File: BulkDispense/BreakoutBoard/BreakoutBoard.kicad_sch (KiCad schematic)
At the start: 30 parts, among them J1 PS, J10 R0~R5, J11 WL1, J12 WL2, J13 DigitalOUT 0~3, J14 DigitalOUT 4~7, J15 WB1, J16 WB2, J17 AnalogIOs, J18 WB-MV1&2, J19 WB-MV3&4, J2 MV1&2, J20 FS1, J21 FS2~FS4, J22 WB-MV5&6, J24 LDS, J3 MV3&4, J4 RV1~4, J5 PCV, J6 FS1, J7 FS3, J8 FS2, J9 FS4

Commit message: Add updated layout
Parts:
- removed J11: WL1, PartsLibrary:CONN_37203-62A3-003PL_3MM, symbol Connector:Conn_01x03_Socket
- removed J12: WL2, PartsLibrary:CONN_37203-62A3-003PL_3MM, symbol Connector:Conn_01x03_Socket
- removed J15: WB1, PartsLibrary:CONN_37203-62A3-003PL_3MM, symbol Connector:Conn_01x03_Socket
- removed J16: WB2, PartsLibrary:CONN_37203-62A3-003PL_3MM, symbol Connector:Conn_01x03_Socket
- removed J22: WB-MV5&6, PartsLibrary:CONN_37203-62A3-003PL_3MM, symbol Connector:Conn_01x03_Socket
- added J11: WL1, PartsLibrary:CONN_37204-62A3-004PL_3MM, symbol Connector:Conn_01x04_Socket
- added J12: WL2, PartsLibrary:CONN_37204-62A3-004PL_3MM, symbol Connector:Conn_01x04_Socket
- added J15: WB1, PartsLibrary:CONN_37204-62A3-004PL_3MM, symbol Connector:Conn_01x04_Socket
- added J16: WB2, PartsLibrary:CONN_37204-62A3-004PL_3MM, symbol Connector:Conn_01x04_Socket
- added J22: WB-MV5&6, PartsLibrary:CONN_37204-62A3-004PL_3MM, symbol Connector:Conn_01x04_Socket
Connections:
- net +24V: now also J11.1 (Pin_1), J12.1 (Pin_1), J15.1 (Pin_1), J16.1 (Pin_1)
- net AI4: now also J15.3 (Pin_3)
- net AI5: now also J16.3 (Pin_3)
- net AI6: now also J11.3 (Pin_3)
- net AI7: now also J12.3 (Pin_3)
- net GND: now also J11.2 (Pin_2), J12.2 (Pin_2), J15.2 (Pin_2), J16.2 (Pin_2)
- net R4_OUT: now also J22.1 (Pin_1)
- net R5_OUT: now also J22.3 (Pin_3)
- no-connect marks 2 -> 7

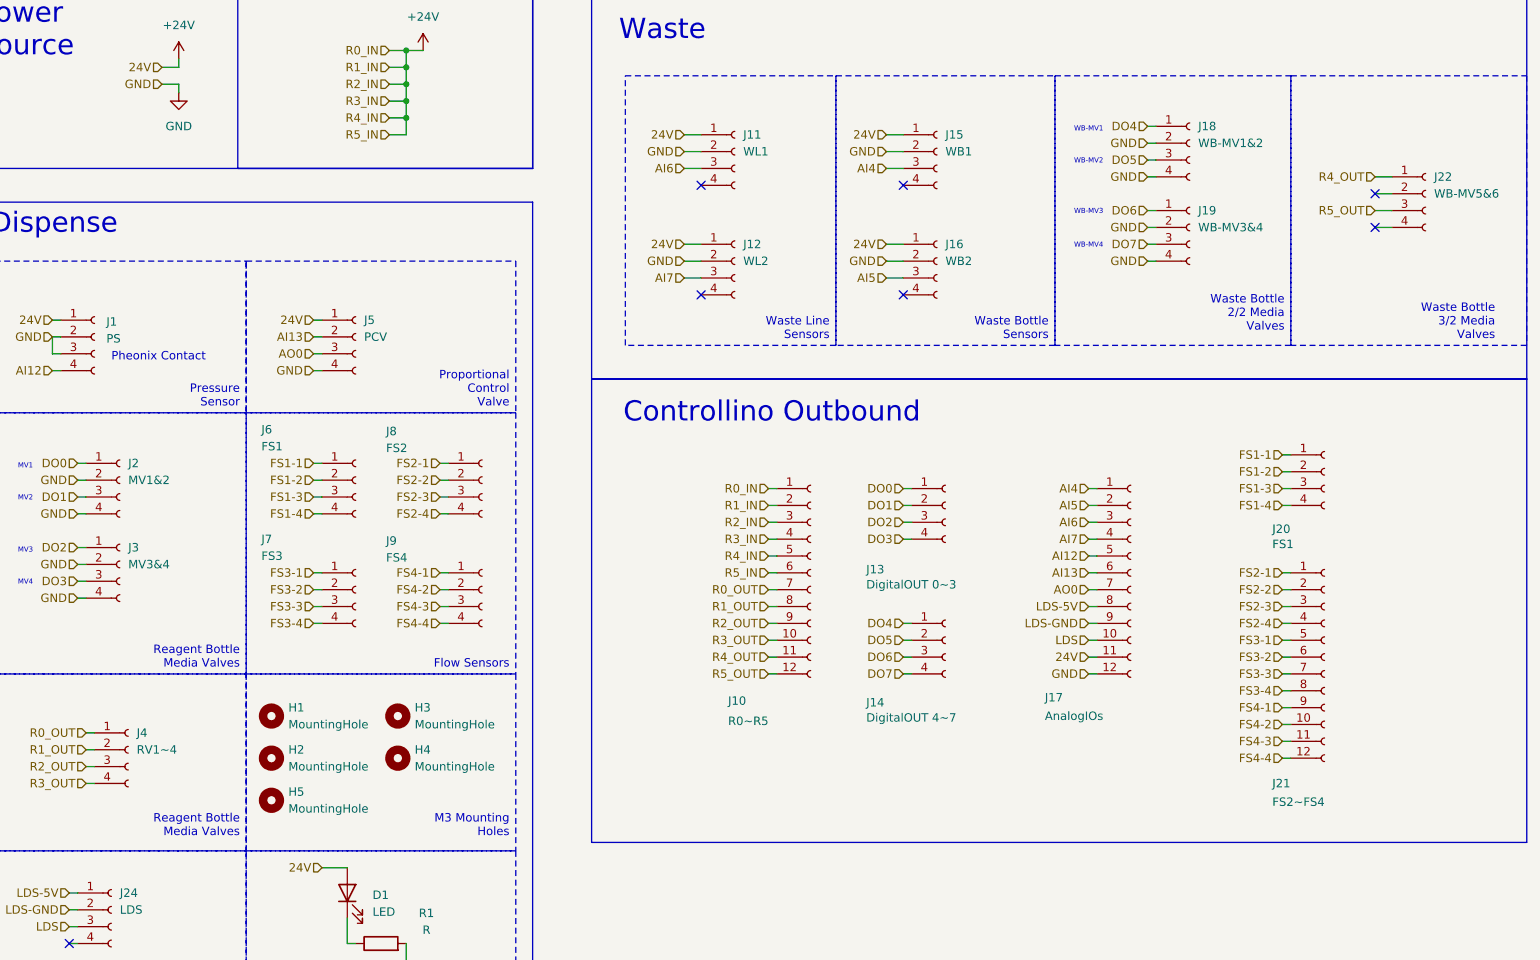
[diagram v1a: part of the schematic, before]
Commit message: Add PCB Revisions
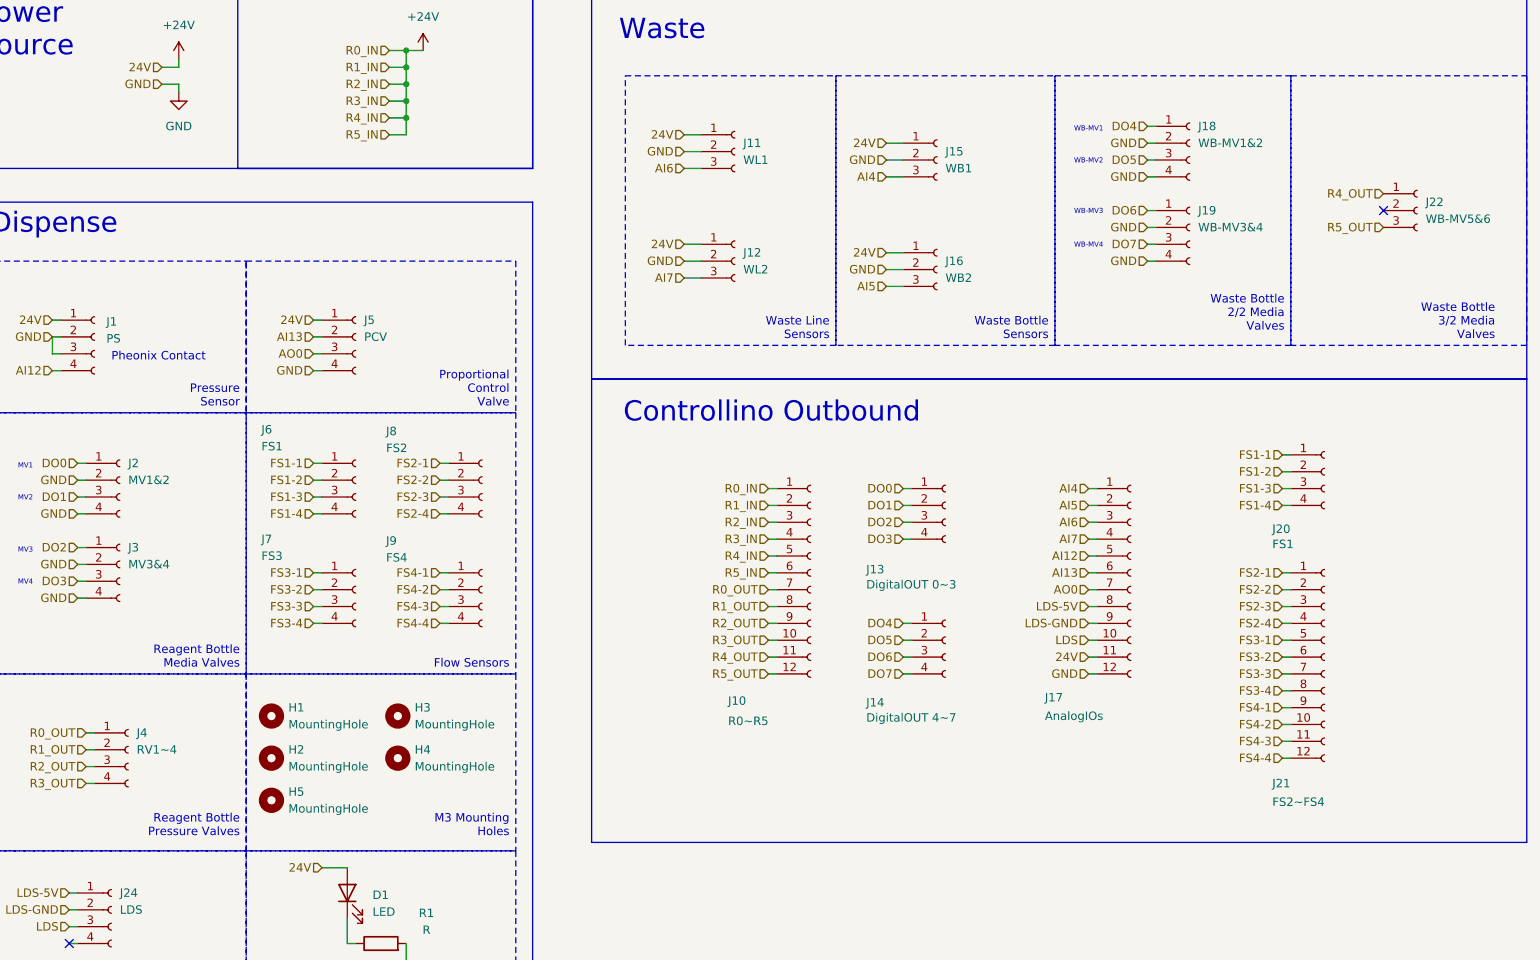
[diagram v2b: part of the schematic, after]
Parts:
- removed J11: WL1, PartsLibrary:CONN_37204-62A3-004PL_3MM, symbol Connector:Conn_01x04_Socket
- removed J12: WL2, PartsLibrary:CONN_37204-62A3-004PL_3MM, symbol Connector:Conn_01x04_Socket
- removed J15: WB1, PartsLibrary:CONN_37204-62A3-004PL_3MM, symbol Connector:Conn_01x04_Socket
- removed J16: WB2, PartsLibrary:CONN_37204-62A3-004PL_3MM, symbol Connector:Conn_01x04_Socket
- removed J22: WB-MV5&6, PartsLibrary:CONN_37204-62A3-004PL_3MM, symbol Connector:Conn_01x04_Socket
- added J11: WL1, PartsLibrary:CONN_37203-62A3-003PL_3MM, symbol Connector:Conn_01x03_Socket
- added J12: WL2, PartsLibrary:CONN_37203-62A3-003PL_3MM, symbol Connector:Conn_01x03_Socket
- added J15: WB1, PartsLibrary:CONN_37203-62A3-003PL_3MM, symbol Connector:Conn_01x03_Socket
- added J16: WB2, PartsLibrary:CONN_37203-62A3-003PL_3MM, symbol Connector:Conn_01x03_Socket
- added J22: WB-MV5&6, PartsLibrary:CONN_37203-62A3-003PL_3MM, symbol Connector:Conn_01x03_Socket
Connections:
- net +24V: now also J11.1 (Pin_1), J12.1 (Pin_1), J15.1 (Pin_1), J16.1 (Pin_1)
- net AI4: now also J15.3 (Pin_3)
- net AI5: now also J16.3 (Pin_3)
- net AI6: now also J11.3 (Pin_3)
- net AI7: now also J12.3 (Pin_3)
- net GND: now also J11.2 (Pin_2), J12.2 (Pin_2), J15.2 (Pin_2), J16.2 (Pin_2)
- net R4_OUT: now also J22.1 (Pin_1)
- net R5_OUT: now also J22.3 (Pin_3)
- no-connect marks 7 -> 2

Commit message: Add New Design
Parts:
- removed J10: R0~R5, PartsLibrary:CONN_37212-62M3-003PL_3MM, symbol Connector:Conn_01x12_Socket
- removed J13: DigitalOUT 0~3, PartsLibrary:CONN_37204-62A3-004PL_3MM, symbol Connector:Conn_01x04_Socket
- removed J14: DigitalOUT 4~7, PartsLibrary:CONN_37204-62A3-004PL_3MM, symbol Connector:Conn_01x04_Socket
- removed J17: AnalogIOs, PartsLibrary:CONN_37212-62M3-003PL_3MM, symbol Connector:Conn_01x12_Socket
- removed J18: WB-MV1&2, PartsLibrary:CONN_37204-62A3-004PL_3MM, symbol Connector:Conn_01x04_Socket
- removed J19: WB-MV3&4, PartsLibrary:CONN_37204-62A3-004PL_3MM, symbol Connector:Conn_01x04_Socket
- removed J2: MV1&2, PartsLibrary:CONN_37204-62A3-004PL_3MM, symbol Connector:Conn_01x04_Socket
- removed J20, J6: FS1, PartsLibrary:CONN_37204-62A3-004PL_3MM, symbol Connector:Conn_01x04_Socket
- removed J21: FS2~FS4, PartsLibrary:CONN_37212-62M3-003PL_3MM, symbol Connector:Conn_01x12_Socket
- removed J22: WB-MV5&6, PartsLibrary:CONN_37203-62A3-003PL_3MM, symbol Connector:Conn_01x03_Socket
- removed J24: LDS, PartsLibrary:CONN_37204-62A3-004PL_3MM, symbol Connector:Conn_01x04_Socket
- removed J3: MV3&4, PartsLibrary:CONN_37204-62A3-004PL_3MM, symbol Connector:Conn_01x04_Socket
- removed J4: RV1~4, PartsLibrary:CONN_37204-62A3-004PL_3MM, symbol Connector:Conn_01x04_Socket
- removed J7: FS3, PartsLibrary:CONN_37204-62A3-004PL_3MM, symbol Connector:Conn_01x04_Socket
- removed J8: FS2, PartsLibrary:CONN_37204-62A3-004PL_3MM, symbol Connector:Conn_01x04_Socket
- removed J9: FS4, PartsLibrary:CONN_37204-62A3-004PL_3MM, symbol Connector:Conn_01x04_Socket
- added C1: 10uF, symbol Device:C
- added C10, C11, C4, C7: 22uF, symbol Device:C
- added C2, C6: 0.1uF, symbol Device:C
- added C3, C5, C8, C9: 4.7uF, symbol Device:C
- added D3, D4: LED, LED_SMD:LED_0201_0603Metric, symbol Device:LED
- added J10: FS1, symbol Connector:Conn_01x06_Socket
- added J13: FS2, symbol Connector:Conn_01x06_Socket
- added J14: FS3, symbol Connector:Conn_01x06_Socket
- added J17: FS4, symbol Connector:Conn_01x06_Socket
- added J20: WB1, PartsLibrary:CONN_37203-62A3-003PL_3MM, symbol Connector:Conn_01x03_Socket
- added J24: WB-MV5, PartsLibrary:CONN_37203-62A3-003PL_3MM, symbol Connector:Conn_01x03_Socket
- added J32: I2C-1, symbol Connector:Conn_01x04_Pin
- added J33: I2C-3, symbol Connector:Conn_01x04_Pin
- added J34: I2C-2, symbol Connector:Conn_01x04_Pin
- added J35: I2C-4, symbol Connector:Conn_01x04_Pin
- added J36: WB-MV6, PartsLibrary:CONN_37203-62A3-003PL_3MM, symbol Connector:Conn_01x03_Socket
- added J37: RV1, PartsLibrary:CONN_37203-62A3-003PL_3MM, symbol Connector:Conn_01x03_Socket
- added J38: RV3, PartsLibrary:CONN_37203-62A3-003PL_3MM, symbol Connector:Conn_01x03_Socket
- added J39: RV2, PartsLibrary:CONN_37203-62A3-003PL_3MM, symbol Connector:Conn_01x03_Socket
- added J4: Signal, PartsLibrary:CONN26_D13-ST-BK_SUL, symbol Connector_Generic:Conn_01x26
- added J40: RV4, PartsLibrary:CONN_37203-62A3-003PL_3MM, symbol Connector:Conn_01x03_Socket
- added J41: MV1, PartsLibrary:CONN_37203-62A3-003PL_3MM, symbol Connector:Conn_01x03_Socket
- added J42: MV2, PartsLibrary:CONN_37203-62A3-003PL_3MM, symbol Connector:Conn_01x03_Socket
- added J43: MV3, PartsLibrary:CONN_37203-62A3-003PL_3MM, symbol Connector:Conn_01x03_Socket
- added J44: MV4, PartsLibrary:CONN_37203-62A3-003PL_3MM, symbol Connector:Conn_01x03_Socket
- added J45: WB-MV1, PartsLibrary:CONN_37203-62A3-003PL_3MM, symbol Connector:Conn_01x03_Socket
- added J46: WB-MV3, PartsLibrary:CONN_37203-62A3-003PL_3MM, symbol Connector:Conn_01x03_Socket
- added J47: WB-MV2, PartsLibrary:CONN_37203-62A3-003PL_3MM, symbol Connector:Conn_01x03_Socket
- added J48: WB-MV4, PartsLibrary:CONN_37203-62A3-003PL_3MM, symbol Connector:Conn_01x03_Socket
- added JP1, JP2, JP3, JP4, JP5, JP6, JP7, JP8: Jumper_2_Open, Connector_PinHeader_1.00mm:PinHeader_1x02_P1.00mm_Vertical, symbol Jumper:Jumper_2_Open
- added L1: 6.8uH, symbol Device:L
- added L2: 5.6uH, symbol Device:L
- added R2: 10k, symbol Device:R
- added R3, R4: R, Resistor_SMD:R_0805_2012Metric, symbol Device:R
- added R5, R7: 100k, symbol Device:R
- added R6: 13.7k, symbol Device:R
- added R8: 22.1k, symbol Device:R
- added TP1, TP2, TP4, TP5: TestPoint, symbol Connector:TestPoint
- added U1: TCA9548APWR, Package_SO:TSSOP-24_4.4x7.8mm_P0.65mm, symbol Interface_Expansion:TCA9548APWR
- added U2, U3: LMR51430, Package_TO_SOT_SMD:SOT-23-6, symbol Regulator_Switching:LMR51430
- added U4: TVS2700DRV, Package_SON:WSON-6-1EP_2x2mm_P0.65mm_EP1x1.6mm, symbol Power_Protection:TVS2700DRV
- D1: footprint LED_SMD:LED_1206_3216Metric -> LED_SMD:LED_0201_0603Metric
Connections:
- net +24V: now also C3.1, C5.1, C8.1, C9.1, J4.1 (Pin_1), TP1.1, U2.3 (VIN), U2.5 (EN), U3.3 (VIN), U3.5 (EN), U4.4 (IN), U4.5 (IN), U4.6 (IN)
- net AI12: now also J4.21 (Pin_21)
- net AI13: now also J4.22 (Pin_22)
- net AI4: now also J4.17 (Pin_17)
- net AI5: now also J4.18 (Pin_18)
- net AI6: now also J4.19 (Pin_19)
- net AI7: now also J4.20 (Pin_20)
- net AO0: now also J4.23 (Pin_23)
- net DO0: now also J4.9 (Pin_9), J41.1 (Pin_1)
- net DO1: now also J4.10 (Pin_10), J42.1 (Pin_1)
- net DO2: now also J4.11 (Pin_11), J43.1 (Pin_1)
- net DO3: now also J4.12 (Pin_12), J44.1 (Pin_1)
- net DO4: now also J4.13 (Pin_13), J45.1 (Pin_1)
- net DO5: now also J4.14 (Pin_14), J47.1 (Pin_1)
- net DO6: now also J4.15 (Pin_15), J46.1 (Pin_1)
- net DO7: now also J4.16 (Pin_16), J48.1 (Pin_1)
- net GND: now also C1.2, C10.2, C11.2, C3.2, C4.2, C5.2, C7.2, C8.2, C9.2, J10.1 (Pin_1), J10.4 (Pin_4), J13.1 (Pin_1), J13.4 (Pin_4), J14.1 (Pin_1), J14.4 (Pin_4), J17.1 (Pin_1), J17.4 (Pin_4), J20.2 (Pin_2), J24.3 (Pin_3), J32.2 (Pin_2), J33.2 (Pin_2), J34.2 (Pin_2), J35.2 (Pin_2), J36.3 (Pin_3), J37.3 (Pin_3), J38.3 (Pin_3), J39.3 (Pin_3), J4.2 (Pin_2), J40.3 (Pin_3), J41.3 (Pin_3), J42.3 (Pin_3), J43.3 (Pin_3), J44.3 (Pin_3), J45.3 (Pin_3), J46.3 (Pin_3), J47.3 (Pin_3), J48.3 (Pin_3), R3.2, R4.2, R6.2, R8.2, TP2.1, U1.1 (A0), U1.12 (GND), U1.2 (A1), U1.21 (A2), U2.1 (GND), U3.1 (GND), U4.1 (GND), U4.2 (GND), U4.3 (GND), U4.7 (GND)
- net LDS: now also J20.3 (Pin_3), J4.24 (Pin_24)
- net R0_OUT: now also J37.1 (Pin_1), J4.3 (Pin_3)
- net R1_OUT: now also J39.1 (Pin_1), J4.4 (Pin_4)
- net R2_OUT: now also J38.1 (Pin_1), J4.5 (Pin_5)
- net R3_OUT: now also J4.6 (Pin_6), J40.1 (Pin_1)
- net R4_OUT: now also J24.1 (Pin_1), J4.7 (Pin_7)
- net R5_OUT: now also J36.1 (Pin_1), J4.8 (Pin_8)
- new net: J33.1 (Pin_1), JP5.2 (B), JP6.2 (B)
- new net: C2.1, U2.6 (CB)
- new net: C2.2, L1.1, R5.1, U2.2 (SW)
- new net: J35.1 (Pin_1), JP7.2 (B), JP8.2 (B)
- new net: J34.1 (Pin_1), JP3.2 (B), JP4.2 (B)
- new net: J32.1 (Pin_1), JP1.2 (B), JP2.2 (B)
- new net: C6.1, U3.6 (CB)
- new net: C6.2, L2.1, R7.1, U3.2 (SW)
- new net: D4.1 (K), R4.1
- new net: R7.2, R8.1, U3.4 (FB)
- new net: R2.2, U1.3 (~{RESET})
- new net: R5.2, R6.1, U2.4 (FB)
- new net: D3.1 (K), R3.1
- new net +3.3V: C1.1, C11.1, C7.1, D4.2 (A), J10.3 (Pin_3), J13.3 (Pin_3), J14.3 (Pin_3), J17.3 (Pin_3), JP1.1 (A), JP4.1 (A), JP6.1 (A), JP8.1 (A), L2.2, R2.1, TP4.1, U1.24 (VCC)
- new net +5V: C10.1, C4.1, D3.2 (A), J20.1 (Pin_1), JP2.1 (A), JP3.1 (A), JP5.1 (A), JP7.1 (A), L1.2, TP5.1
- new net FS1-SCL: J10.5 (Pin_5), U1.5 (SC0)
- new net FS1-SDA: J10.2 (Pin_2), U1.4 (SD0)
- new net FS2-SCL: J13.5 (Pin_5), U1.7 (SC1)
- new net FS2-SDA: J13.2 (Pin_2), U1.6 (SD1)
- new net FS3-SCL: J14.5 (Pin_5), U1.9 (SC2)
- new net FS3-SDA: J14.2 (Pin_2), U1.8 (SD2)
- new net FS4-SCL: J17.5 (Pin_5), U1.11 (SC3)
- new net FS4-SDA: J17.2 (Pin_2), U1.10 (SD3)
- new net SC4: J32.3 (Pin_3), U1.14 (SC4)
- new net SC5: J34.3 (Pin_3), U1.16 (SC5)
- new net SC6: J33.3 (Pin_3), U1.18 (SC6)
- new net SC7: J35.3 (Pin_3), U1.20 (SC7)
- new net SCL: J4.25 (Pin_25), U1.22 (SCL)
- new net SD4: J32.4 (Pin_4), U1.13 (SD4)
- new net SD5: J34.4 (Pin_4), U1.15 (SD5)
- new net SD6: J33.4 (Pin_4), U1.17 (SD6)
- new net SD7: J35.4 (Pin_4), U1.19 (SD7)
- new net SDA: J4.26 (Pin_26), U1.23 (SDA)
- no-connect marks 2 -> 18
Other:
- note added: "24V"
- note added: "3V3"
- note added: "5V"
- note added: "Extra I2C Pins"
- note added: "Flow Sensors"
- note added: "I2C Multiplexer"
- note added: "LED"
- note removed: "MV1"
- note removed: "MV2"
- note removed: "MV3"
- note removed: "MV4"
- note removed: "WB-MV1"
- note removed: "WB-MV2"
- note removed: "WB-MV3"
- note removed: "WB-MV4"
- moved on the sheet: D1, H1, H2, H3, H4, H5, J1, J11, J12, J15, J16, J5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

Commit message: Start PCB Routing
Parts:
- added R10, R14, R15, R16, R17, R18, R19, R20, R21, R22, R23, R24, R25, R26, R27, R28, R29, R9: 4.7k, Resistor_SMD:R_0402_1005Metric, symbol Device:R
- added R11, R12, R13: 0, Resistor_SMD:R_0402_1005Metric, symbol Device:R
- C1, C2, C6: footprint (none) -> Capacitor_SMD:C_01005_0402Metric
- C10, C11, C3, C4, C5, C7, C8, C9: footprint (none) -> Capacitor_SMD:C_0805_2012Metric
- J10, J13, J14, J17: footprint (none) -> Connector_Molex:Molex_PicoBlade_53047-0610_1x06_P1.25mm_Vertical
- J32, J33, J34, J35: footprint (none) -> PartsLibrary:CONN_37204-62A3-004PL_3MM
- L1: footprint (none) -> Inductor_SMD:L_Bourns_SRP7028A_7.3x6.6mm
- L2: footprint (none) -> PartsLibrary:IND_IHLP-2020CZ
- R1: value R -> 2.2k; MPN ERJ-P06J122V -> CRCW12062K20FKEA
- R2: footprint (none) -> Resistor_SMD:R_0402_1005Metric
- R3: value R -> 330; MPN ERJ-P06J122V -> RC0603FR-07330RL
- R4: value R -> 150; MPN ERJ-P06J122V -> CRCW0603150RFKEA
- R5, R7, R8: footprint (none) -> Resistor_SMD:R_0603_1608Metric
- R6: footprint (none) -> Capacitor_SMD:C_0603_1608Metric
- TP1, TP4, TP5: footprint (none) -> TestPoint:TestPoint_THTPad_D1.0mm_Drill0.5mm
- TP2: footprint (none) -> TestPoint:TestPoint_THTPad_1.0x1.0mm_Drill0.5mm
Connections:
- net +3.3V: now also R10.2, R14.2, R15.2, R16.2, R17.2, R18.2, R19.2, R20.2, R21.1, R22.1, R23.1, R24.1, R25.1, R26.1, R27.1, R28.2, R29.1, R9.2
- net FS1-SCL: now also R14.1
- net FS1-SDA: now also R15.1
- net FS2-SCL: now also R16.1
- net FS2-SDA: now also R17.1
- net FS3-SCL: now also R18.1
- net FS3-SDA: now also R19.1
- net FS4-SCL: now also R20.1
- net FS4-SDA: now also R28.1
- net GND: now also R11.1, R11.2, R12.1, R12.2, R13.1, R13.2
- net SC4: now also R29.2
- net SC5: now also R22.2
- net SC6: now also R24.2
- net SC7: now also R26.2
- net SCL: now also R9.1
- net SD4: now also R21.2
- net SD5: now also R23.2
- net SD6: now also R25.2
- net SD7: now also R27.2
- net SDA: now also R10.1
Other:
- note added: "4.7k Pull-Up Resistors"
- moved on the sheet: J10, J13, J14, J17, J32, J33, J34, J35, JP1, JP2, JP3, JP4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

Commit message: Start I2C Layout
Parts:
- removed R21, R22, R23, R24, R25, R26, R27, R29: 4.7k, Resistor_SMD:R_0402_1005Metric, symbol Device:R
- J32, J33, J34, J35, JP1, JP2, JP3, JP4, JP5, JP6, JP7, JP8: now not fitted

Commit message: Finalized Draft - BreakoutBoard
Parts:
- C2, C6: footprint Capacitor_SMD:C_01005_0402Metric -> Capacitor_SMD:C_0603_1608Metric
- J20: value WB1 -> LDS
- J24: value WB-MV5 -> WB-MV1
- J36: value WB-MV6 -> WB-MV2
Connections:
- net AI12: now also J4.10 (Pin_10); no longer J4.21 (Pin_21)
- net AI13: now also J4.11 (Pin_11); no longer J4.22 (Pin_22)
- net AI4: now also J4.6 (Pin_6); no longer J4.17 (Pin_17)
- net AI5: now also J4.7 (Pin_7); no longer J4.18 (Pin_18)
- net AI6: now also J4.8 (Pin_8); no longer J4.19 (Pin_19)
- net AI7: now also J4.9 (Pin_9); no longer J4.20 (Pin_20)
- net AO0: now also J4.12 (Pin_12); no longer J4.23 (Pin_23)
- net DO0: now also J4.19 (Pin_19); no longer J4.9 (Pin_9)
- net DO1: now also J4.20 (Pin_20); no longer J4.10 (Pin_10)
- net DO2: now also J4.21 (Pin_21); no longer J4.11 (Pin_11)
- net DO3: now also J4.22 (Pin_22); no longer J4.12 (Pin_12)
- net DO4: now also J4.23 (Pin_23); no longer J4.13 (Pin_13)
- net DO5: now also J4.24 (Pin_24); no longer J4.14 (Pin_14)
- net DO6: now also J4.25 (Pin_25); no longer J4.15 (Pin_15)
- net DO7: now also J4.26 (Pin_26); no longer J4.16 (Pin_16)
- net LDS: now also J4.5 (Pin_5); no longer J4.24 (Pin_24)
- net R0_OUT: now also J4.13 (Pin_13); no longer J4.3 (Pin_3)
- net R1_OUT: now also J4.14 (Pin_14); no longer J4.4 (Pin_4)
- net R2_OUT: now also J4.15 (Pin_15); no longer J4.5 (Pin_5)
- net R3_OUT: now also J4.16 (Pin_16); no longer J4.6 (Pin_6)
- net R4_OUT: now also J4.17 (Pin_17); no longer J4.7 (Pin_7)
- net R5_OUT: now also J4.18 (Pin_18); no longer J4.8 (Pin_8)
- net SCL: now also J4.4 (Pin_4); no longer J4.25 (Pin_25)
- net SDA: now also J4.3 (Pin_3); no longer J4.26 (Pin_26)

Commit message: Final Update
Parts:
- C1: footprint Capacitor_SMD:C_01005_0402Metric -> Capacitor_SMD:C_0402_1005Metric
- D1, D3, D4: footprint LED_SMD:LED_0201_0603Metric -> LED_SMD:LED_0603_1608Metric
- R1: footprint Resistor_SMD:R_0805_2012Metric -> Resistor_SMD:R_1206_3216Metric
- R3, R4: footprint Resistor_SMD:R_0805_2012Metric -> Resistor_SMD:R_0603_1608Metric
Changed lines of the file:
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@@
 			)
 		)
-		(property "Datasheet" "https://www.digikey.com/en/products/detail/murata-electronics/grm188r71c104ka01d/587060"
+		(property "Datasheet" "https://www.digikey.com/en/products/detail/murata-electronics/GRM188R72A104KA35D/702826"
 			(at 190.5 34.29 0)
 			(effects
@@
 			)
 		)
-		(property "Footprint" "LED_SMD:LED_0201_0603Metric"
+		(property "Footprint" "LED_SMD:LED_0603_1608Metric"
 			(at 138.43 198.12 0)
 			(effects
@@
 			)
 		)
-		(property "Datasheet" "https://www.digikey.com/en/products/detail/murata-electronics/grm188r71c104ka01d/587060"
+		(property "Datasheet" "https://www.digikey.com/en/products/detail/murata-electronics/GRM188R72A104KA35D/702826"
 			(at 327.66 34.29 0)
 			(effects
@@
 			)
 		)
-		(property "Footprint" "Resistor_SMD:R_0805_2012Metric"
+		(property "Footprint" "Resistor_SMD:R_0603_1608Metric"
 			(at 143.51 255.778 90)
 			(effects
@@
 			)
 		)
-		(property "Footprint" "Capacitor_SMD:C_01005_0402Metric"
+		(property "Footprint" "Capacitor_SMD:C_0402_1005Metric"
 			(at 301.9552 118.11 0)
 			(effects
@@
 			)
 		)
-		(property "Footprint" "Resistor_SMD:R_0805_2012Metric"
+		(property "Footprint" "Resistor_SMD:R_0603_1608Metric"
 			(at 143.51 231.648 90)
 			(effects
@@
 			)
 		)
-		(property "Footprint" "LED_SMD:LED_0201_0603Metric"
+		(property "Footprint" "LED_SMD:LED_0603_1608Metric"
 			(at 138.43 246.38 0)
 			(effects
@@
 			)
 		)
-		(property "Footprint" "LED_SMD:LED_0201_0603Metric"
+		(property "Footprint" "LED_SMD:LED_0603_1608Metric"
 			(at 138.43 222.25 0)
 			(effects
@@
 			)
 		)
-		(property "Footprint" "Resistor_SMD:R_0805_2012Metric"
+		(property "Footprint" "Resistor_SMD:R_1206_3216Metric"
 			(at 143.51 207.518 90)
 			(effects
